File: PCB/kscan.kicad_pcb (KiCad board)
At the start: 2 copper layers, 88.9 x 53.3 mm, 28 parts, among them IC1 ATMEGA328P-A, P1 USB_A, P2 LASER_1, P3 LASER_2, P4 LASER_3, P5 LASER_4, P6 MOTOR_CONN, SW1 RESET, U1 FT232RL, U2 ULN2003A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

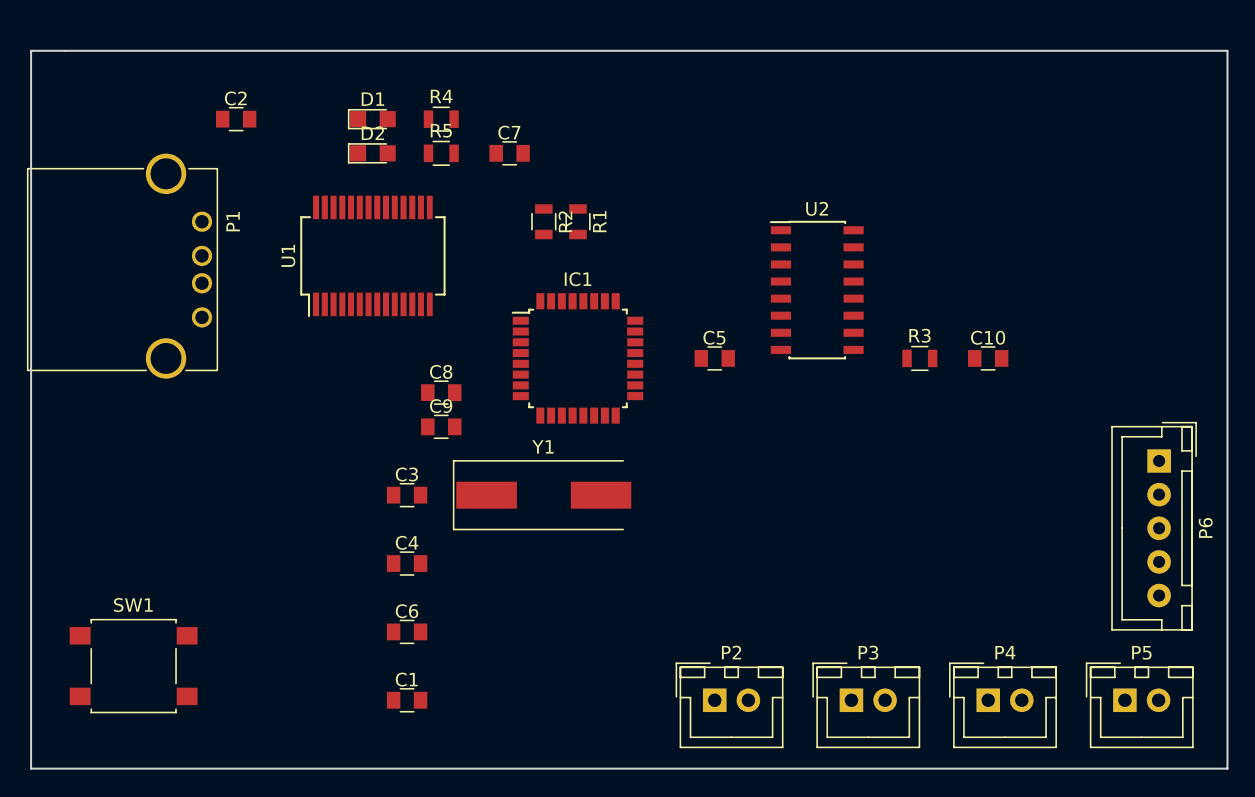
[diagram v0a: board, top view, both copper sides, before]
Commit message: Change pin mapping
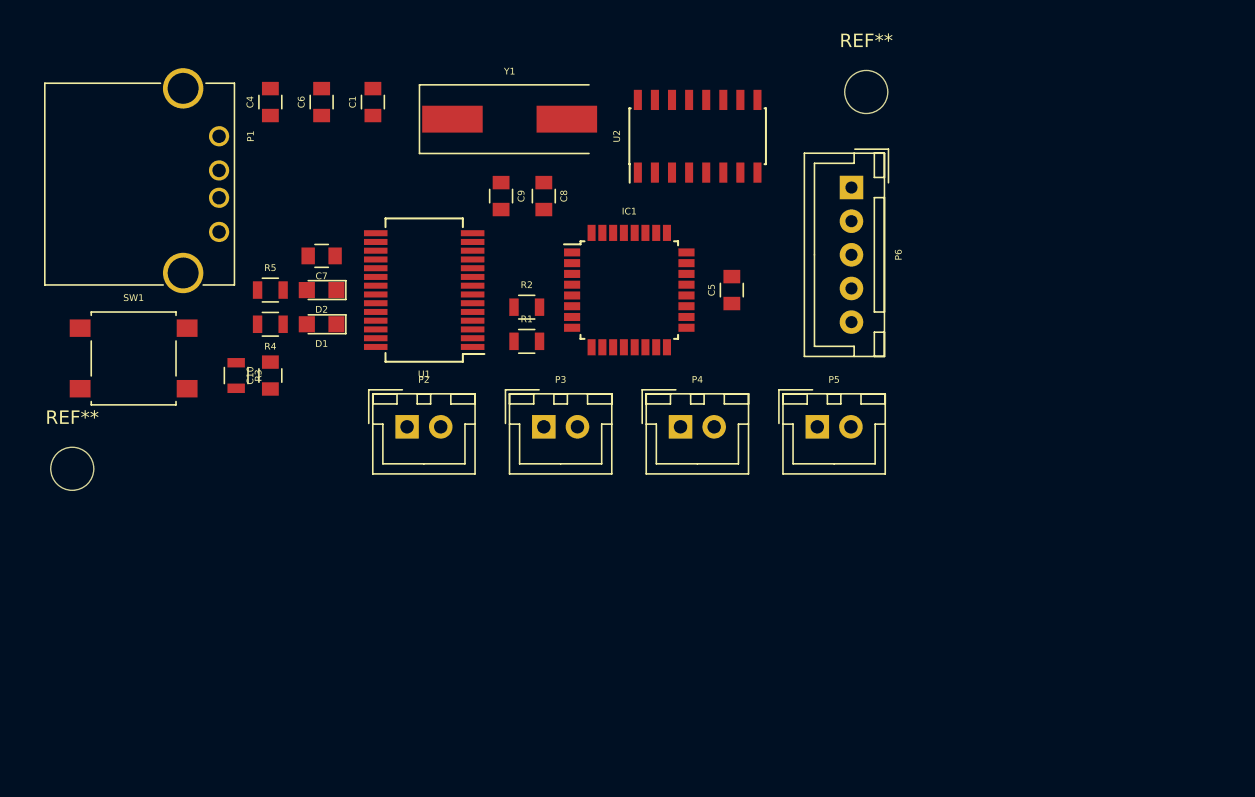
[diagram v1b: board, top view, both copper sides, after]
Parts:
- removed C2: 0.1uF, Capacitors_SMD:C_0805
- removed C3: 4.7uF, Capacitors_SMD:C_0805
- added REF**: M3, Mounting_Holes:MountingHole_3.2mm_M3_DIN965, F.Cu at (90.0, 31.0)
- added REF**: M3, Mounting_Holes:MountingHole_3.2mm_M3_DIN965, F.Cu at (31.0, 59.0)
- moved C10 53.4 mm to (45.7, 52.1), turned to 90 degrees
- moved R3 50.8 mm to (43.2, 52.1), turned to 270 degrees
- moved C1 44.5 mm to (53.3, 31.8), turned to 90 degrees
- moved C6 39.9 mm to (49.5, 31.8), turned to 90 degrees
- moved C4 35.8 mm to (45.7, 31.8), turned to 90 degrees
- moved P3 30.6 mm to (66.0, 55.9)
- moved P4 30.6 mm to (76.2, 55.9)
- moved P5 30.6 mm to (86.4, 55.9)
- moved P6 30.6 mm to (88.9, 38.1)
- moved P2 30.6 mm to (55.9, 55.9)
- moved Y1 28.1 mm to (63.5, 33.0)
- moved SW1 22.9 mm to (35.6, 50.8)
- moved R4 19.8 mm to (45.7, 48.3), turned to 180 degrees
- moved C9 17.7 mm to (62.9, 38.7), turned to 270 degrees
- moved C8 16.5 mm to (66.0, 38.7), turned to 270 degrees
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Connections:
- IC1 pad 25: Net-(IC1-Pad25) -> MC4
- IC1 pad 26: Net-(IC1-Pad26) -> MC3
- IC1 pad 27: Net-(IC1-Pad27) -> MC2
- IC1 pad 28: Net-(IC1-Pad28) -> MC1
- U2 pad 1: Net-(IC1-Pad25) -> MC1
- U2 pad 2: Net-(IC1-Pad26) -> MC2
- U2 pad 3: Net-(IC1-Pad27) -> MC3
- U2 pad 4: Net-(IC1-Pad28) -> MC4
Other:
- board outline removed
